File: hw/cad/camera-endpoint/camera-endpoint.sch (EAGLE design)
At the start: 44 parts, among them IC1 FT232RL, J1 DCJ0202, U1 TPS54231SO8, X1 MINI-USB-UX60-MB-5ST

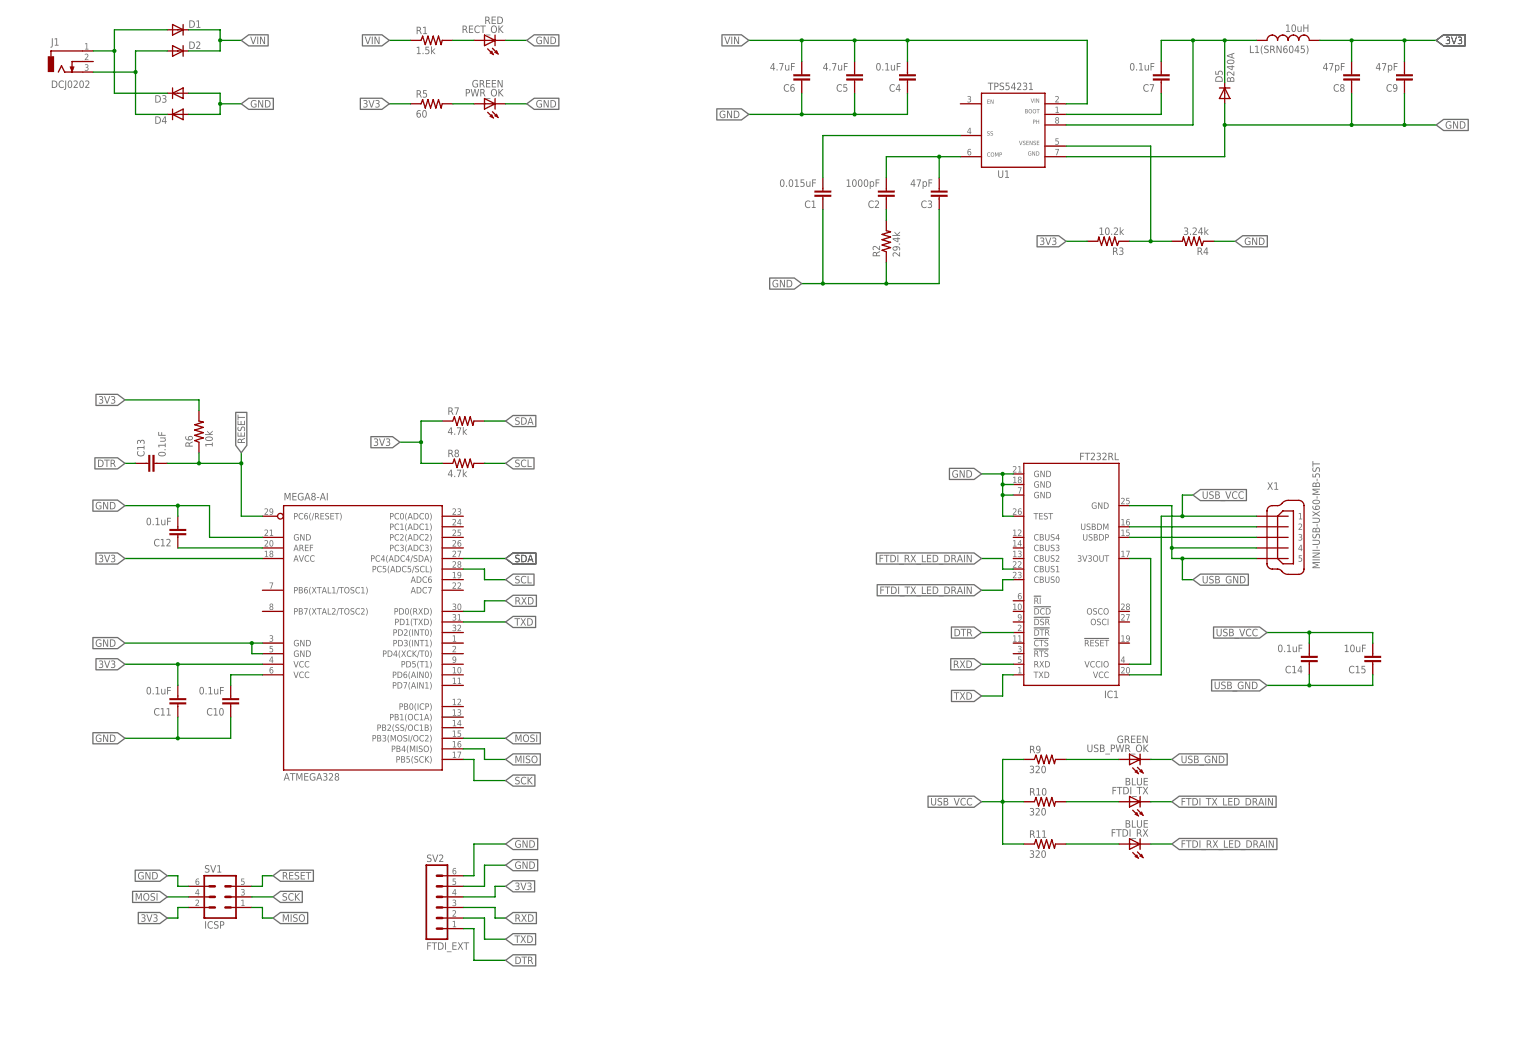
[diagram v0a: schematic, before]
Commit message: cleaned MC/Power sheet, added authoring info
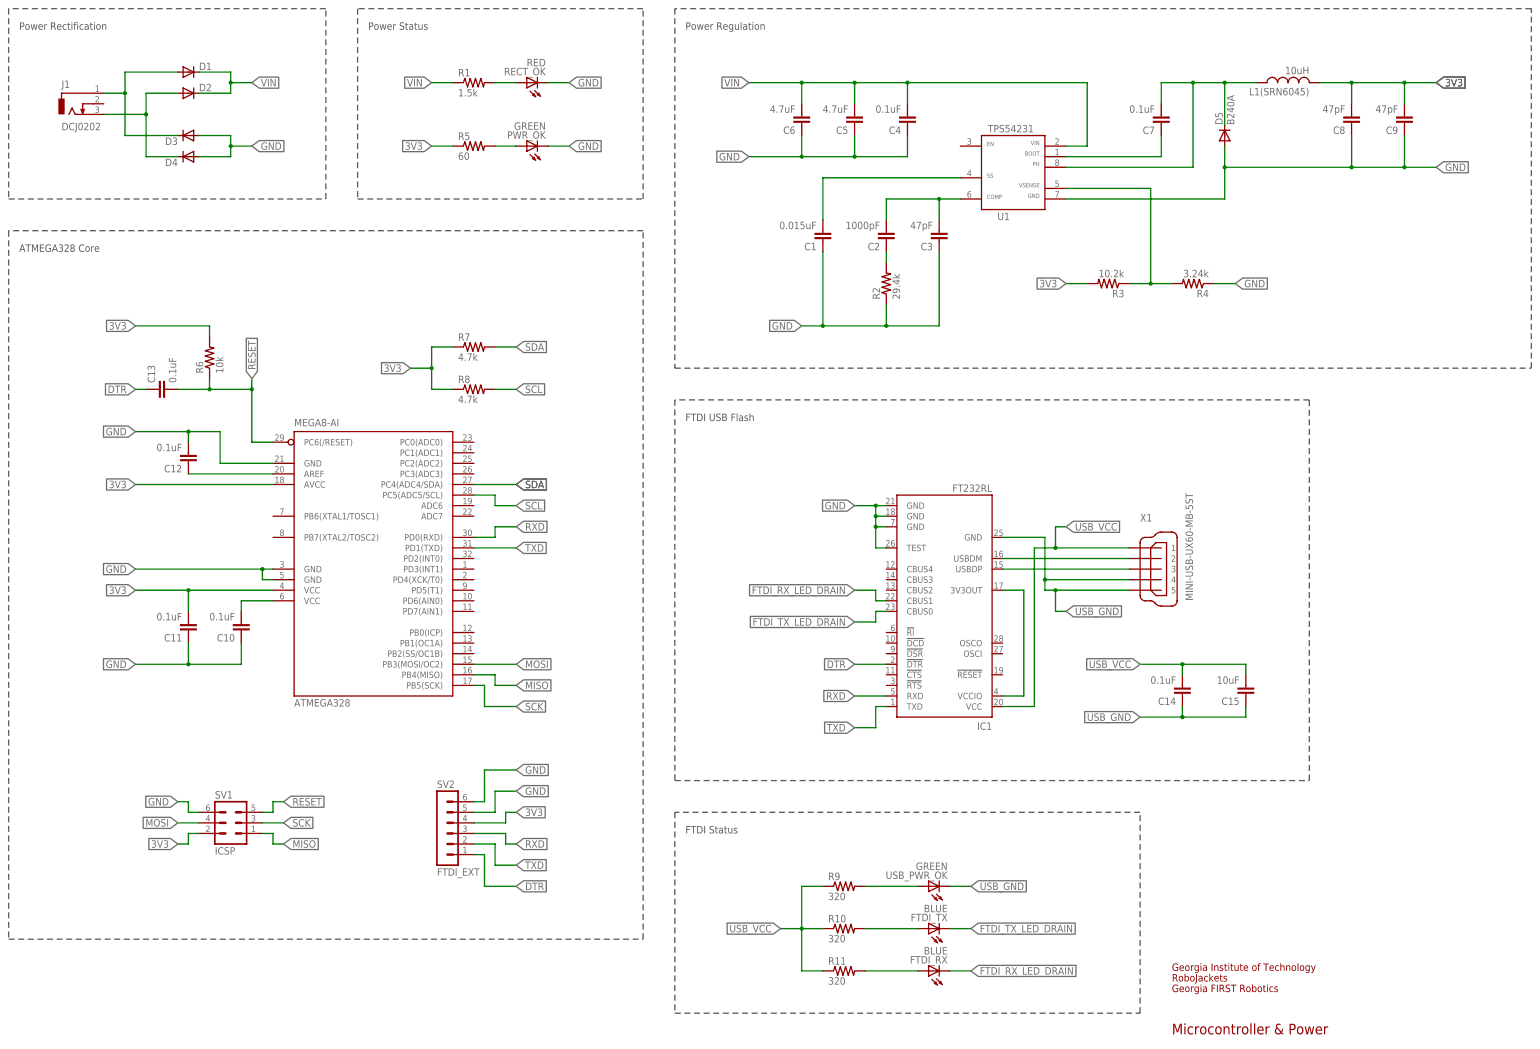
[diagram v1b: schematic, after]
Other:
- note added: "ATMEGA328 Core"
- note added: "FTDI Status"
- note added: "FTDI USB Flash"
- note added: "Georgia FIRST Robotics"
- note added: "Georgia Institute of Technology"
- note added: "Microcontroller & Power"
- note added: "Power Rectification"
- note added: "Power Regulation"
- note added: "Power Status"
- note added: "RoboJackets"
- moved on the sheet: ATMEGA328, C1, C10, C11, C12, C13, C14, C15, C2, C3, C4, C5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

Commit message: refined symbology on sheet 1
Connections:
- net VIN renamed VCC
- new net +3V3: ATMEGA328.AVCC, ATMEGA328.VCC@1, C11.2, C8.2, C9.2, L1(SRN6045).2, R3.2, R5.1, R6.2, R7.1, R8.1
- net 3V3: no longer ATMEGA328.AVCC, ATMEGA328.VCC@1, C11.2, C8.2, C9.2, L1(SRN6045).2, R3.2, R5.1, R6.2, R7.1, R8.1
- net GND: now also C14.1, C15.1, IC1.GND@A, X1.4, X1.5
- net USB_GND: no longer C14.1, C15.1, IC1.GND@A, X1.4, X1.5

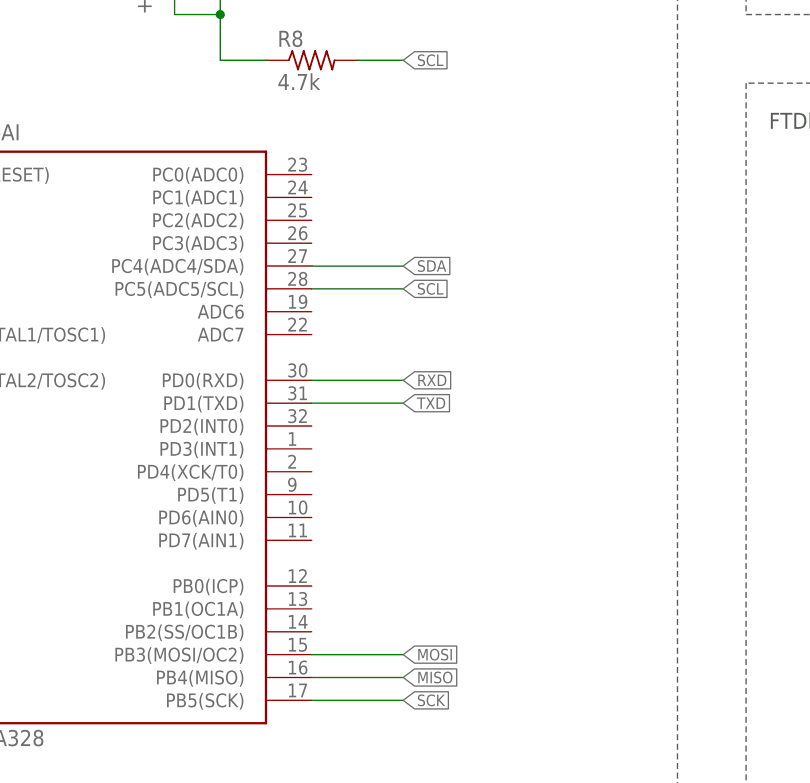
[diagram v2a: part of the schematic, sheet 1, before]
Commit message: finished serial conversion and IO in schematic
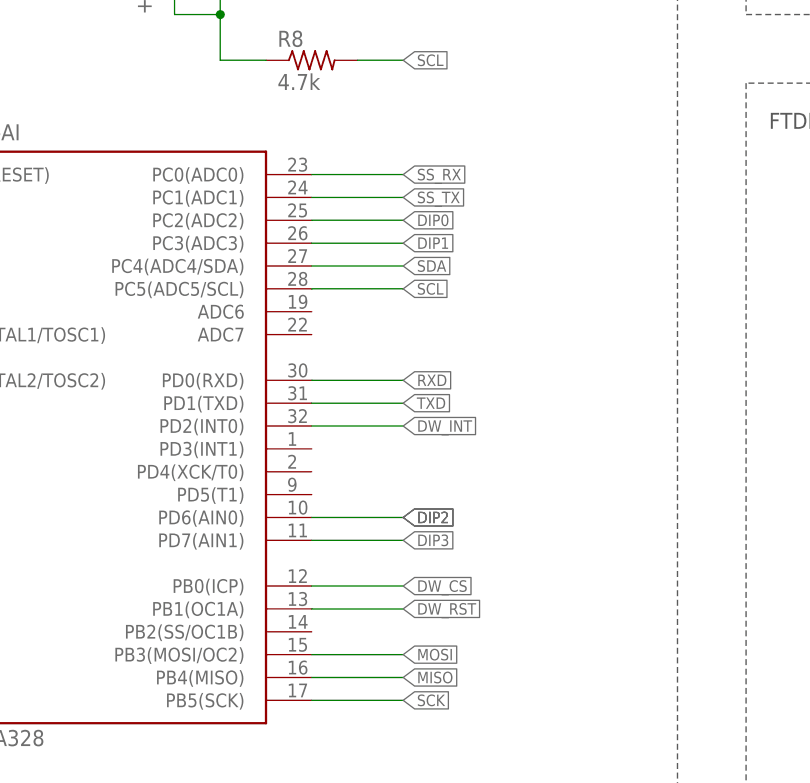
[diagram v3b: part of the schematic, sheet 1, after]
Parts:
- added IC2: MAX3488CSA, maxim:MAX3467CPA
- added J2: SBH11-PBPC-D05-RA, RoboJackets-Connectors:SBH11-PBPC-D05-RA
- added JP1: SER_DBG, pinhead:PINHD-1X2
- added JP2: VCC, pinhead:PINHD-1X2
- added JP3: 3,3, pinhead:PINHD-1X2
- added JP4: I2C, pinhead:PINHD-1X2
- added R12, R13, R14, R15: 10k, resistor:R-US_R0603
- added RS485_RX, RS485_TX: (no value), con-wago-500:W237-102
- added S1: SWS004, smd-special:SWS004
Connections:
- new net DIP0: ATMEGA328.PC2(ADC2), R12.1, S1.1
- new net DIP1: ATMEGA328.PC3(ADC3), R13.1, S1.2
- new net DIP2: ATMEGA328.PD6(AIN0), R14.1, S1.3
- new net DIP3: ATMEGA328.PD7(AIN1), R15.1, S1.4
- new net DW_CS: ATMEGA328.PB0(ICP), J2.10
- new net DW_INT: ATMEGA328.PD2(INT0), J2.3
- new net DW_RST: ATMEGA328.PB1(OC1A), J2.5
- new net RS485_RX_N: IC2.B, RS485_RX-2.KL
- new net RS485_RX_P: IC2.A, RS485_RX-1.KL
- new net RS485_TX_N: IC2.Z, RS485_TX-2.KL
- new net RS485_TX_P: IC2.Y, RS485_TX-1.KL
- new net SS_RX: ATMEGA328.PC0(ADC0), IC2.RO, JP1.2
- new net SS_TX: ATMEGA328.PC1(ADC1), IC2.DI, JP1.1
- net +3V3: now also IC2.VCC, J2.6, JP3.1, S1.5, S1.6, S1.7, S1.8
- net GND: now also IC2.GND, J2.7, JP2.2, JP3.2, R12.2, R13.2, R14.2, R15.2
- net MISO: now also J2.8
- net MOSI: now also J2.2
- net SCK: now also J2.1
- net SCL: now also JP4.2
- net SDA: now also JP4.1
- net VCC: now also JP2.1
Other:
- note added: "I2C Breakout"
- note added: "IO & IO Conversion"
- note added: "Internal Power Breakout"
- note added: "RS232 - RS485 Conversion"
- note added: "Radio Connector"
- note added: "Radio ID Selection"
- note added: "Serial Headers"

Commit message: fixed problems from design review
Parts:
- added C16: 330uF, rcl:CPOL-EUE5-8.5
- added R16, R17: 470, resistor:R-US_R0603
- added R18: 374k 1%, resistor:R-US_R0603
- added R19: 102k 1%, resistor:R-US_R0603
- C2: value 1000pF -> 4700pF
- C8: value 47pF -> 47uF; device resistor:C-EUC0603 -> rcl:C-EUC1206
- D1, D2, D3, D4: value (none) -> SS12
- JP3: value 3,3 -> 3.3V
- R2: value 29.4k -> 21.0k
- R3: value 10.2k -> 10.2k 1%
- R4: value 3.24k -> 3.24k 1%
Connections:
- removed net 3V3: SV1.2, SV2.4
- removed net USB_GND: USB_PWR_OK.C
- new net N$13: IC1.TXD, R17.1
- new net PWR_EN: R18.1, R19.2, U1.3
- net +3V3: now also ATMEGA328.VCC@2, C10.2, SV1.2, SV2.4
- net DW_CS: now also ATMEGA328.PB2(SS/OC1B); no longer ATMEGA328.PB0(ICP)
- net GND: now also C16.-, R19.1, USB_PWR_OK.C
- net N$10: now also IC1.RXD, R16.1; no longer ATMEGA328.VCC@2, C10.2
- net RXD: now also R17.2; no longer IC1.RXD
- net TXD: now also R16.2; no longer IC1.TXD
- net USB_VCC: now also IC1.!RESET
- net VCC: now also C16.+, R18.2
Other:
- moved on the sheet: C4, C5, C6
